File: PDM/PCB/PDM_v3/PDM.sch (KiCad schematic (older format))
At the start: 59 parts, among them IC1 SN74LVC1GU04DBVT, J1 12V BAT, J10 RASPBERRY PI, J11 EMU, J12 Conn_01x02_Male, J13 SAFETY SYSTEM, J16 GND, J2 EMU PIN 21 GN(AUX1), J3 EMU PIN 13 GN (AUX2), J4 BACK LIGHT, J5 COILS, J6 INJECTORS, J7 LSU 4.9, J8 RACE TCS, J9 STM BOX, U1 BTS50010-1TAE, U2 BTS50010-1TAE, U3 BTS50010-1TAE, U4 LM2937xMP

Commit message: Update PDM PCB
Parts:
- removed 12V1: 85 K1 (starter), MountingHole:MountingHole_2.5mm_Pad_Via, symbol Connector:Conn_01x01_Male
- removed C1: 0.2F, Kondensator:Kondensator, symbol Device:C
- removed C6: 0.1uF, Capacitor_SMD:C_0805_2012Metric, symbol Device:C_Small
- removed C7: 10uF, Capacitor_SMD:C_0805_2012Metric, symbol Device:C_Small
- removed D5: D_Schottky, Diode_SMD:D_SOD-123, symbol Device:D_Schottky
- removed IC1: SN74LVC1GU04DBVT, SN74LVC1GU04DBVT:SOT95P280X145-5N, symbol SN74LVC1GU04DBVT:SN74LVC1GU04DBVT
- removed J12: Conn_01x02_Male, Connector_PinHeader_2.54mm:PinHeader_1x02_P2.54mm_Vertical, symbol Connector:Conn_01x02_Male
- removed J13: SAFETY SYSTEM, MountingHole:MountingHole_2.2mm_M2_DIN965_Pad, symbol Connector:Conn_01x01_Male
- removed J2: EMU PIN 21 GN(AUX1), MountingHole:MountingHole_2.2mm_M2_DIN965_Pad, symbol Connector:Conn_01x01_Male
- removed J3: EMU PIN 13 GN (AUX2), MountingHole:MountingHole_2.2mm_M2_DIN965_Pad, symbol Connector:Conn_01x01_Male
- removed R1: 0.1, Resistor_SMD:R_0805_2012Metric, symbol Device:R
- removed U4: LM2937xMP, Package_TO_SOT_SMD:SOT-223-3_TabPin2, symbol Regulator_Linear:LM2937xMP
- added C1, C15, C17, C20, C55: 0.1uF, Capacitor_SMD:C_0603_1608Metric, symbol Device:C_Small
- added C27: 100nF, Capacitor_SMD:C_0805_2012Metric_Pad1.15x1.40mm_HandSolder, symbol Device:C
- added C28: 150nF, Capacitor_SMD:C_0603_1608Metric, symbol Device:C_Small
- added C29: 10nF, Capacitor_SMD:C_0805_2012Metric_Pad1.15x1.40mm_HandSolder, symbol Device:C
- added C30, C31: 100uF, EEETP1C101AP:EEE0JA471UAP, symbol EEETP1C101AP:EEETP1C101AP
- added C47, C54: 0.47uF, Capacitor_SMD:C_0603_1608Metric, symbol Device:C_Small
- added C48: 22uF, Capacitor_SMD:C_0603_1608Metric, symbol Device:C_Small
- added C49, C50: SCMR18H105PRBB0, SCMR18H105PRBB0:SCMR18H105PRBB0, symbol SCMR18H105PRBB0:SCMR18H105PRBB0
- added C51, C52, C56: 1uF, Capacitor_SMD:C_0603_1608Metric, symbol Device:C_Small
- added D9: D_TVS_ALT, Diode_SMD:D_SMA_Handsoldering, symbol Device:D_TVS_ALT
- added IC1, IC10, IC8: BU4S584G2-TR, BU4S584G2-TR:SOT95P280X125-5N, symbol BU4S584G2-TR:BU4S584G2-TR
- added IC7: KF50BDT-TR, KF50BDT-TR:TO228P972X240-3N, symbol KF50BDT-TR:KF50BDT-TR
- added IC9: TMP236A4DBZT, TMP236A4DBZT:SOT95P237X112-3N, symbol TMP236A4DBZT:TMP236A4DBZT
- added J15: SERVO_GEAR, MountingHole:MountingHole_2.2mm_M2_DIN965_Pad, symbol Connector:Conn_01x01_Male
- added J17: SERVO_CLUTCH, MountingHole:MountingHole_2.2mm_M2_DIN965_Pad, symbol Connector:Conn_01x01_Male
- added J2: 90130-1106, 90130-1106:SHDR6W65P254_2X3_996X975X1110P, symbol 90130-1106:90130-1106
- added J3: Conn_01x09_Male, Connector_PinHeader_1.27mm:PinHeader_1x09_P1.27mm_Vertical, symbol Connector:Conn_01x09_Male
- added R1: 22k, Resistor_SMD:R_0603_1608Metric, symbol Device:R_Small
- added R18: 1R, Resistor_SMD:R_0603_1608Metric_Pad1.05x0.95mm_HandSolder, symbol Device:R
- added R19: R_Small, Resistor_SMD:R_0603_1608Metric, symbol Device:R_Small
- added R20: R_Small, Resistor_SMD:R_1210_3225Metric, symbol Device:R_Small
- added R21: 6.8k, Resistor_SMD:R_0603_1608Metric, symbol Device:R_Small
- added R22, R23, R24, R25, R26, R27: 0, Resistor_SMD:R_0603_1608Metric, symbol Device:R_Small
- added SERVO1, SERVO2: 15, Fuse:Fuse_1206_3216Metric, symbol Device:Fuse
- added STM32: 2, Fuse:Fuse_0805_2012Metric, symbol Device:Fuse
- added U7: BTS50010-1TAE, Package_TO_SOT_SMD:TO-263-7_TabPin4, symbol PDM-rescue:BTS50010-1TAE-BTS50010-1TAE-PowerBox-rescue
- added U8: MCP2561-E-SN, Package_SO:SOIC-8_3.9x4.9mm_P1.27mm, symbol Interface_CAN_LIN:MCP2561-E-SN
- BACKLIGHT1: renamed from F2; footprint Fuse:Fuse_1812_4532Metric_Pad1.30x3.40mm_HandSolder -> Fuse:Fuse_1206_3216Metric
- COILS1: renamed from F3; footprint Fuse:Fuse_1812_4532Metric_Pad1.30x3.40mm_HandSolder -> Fuse:Fuse_1206_3216Metric
- DASHBOARD1: renamed from F7; footprint Fuse:Fuse_1812_4532Metric_Pad1.30x3.40mm_HandSolder -> Fuse:Fuse_1206_3216Metric
- EMU1: renamed from F9; footprint Fuse:Fuse_1812_4532Metric_Pad1.30x3.40mm_HandSolder -> Fuse:Fuse_1206_3216Metric
- H1, H2, H3, H4: footprint MountingHole:MountingHole_3.2mm_M3_DIN965_Pad -> MountingHole:MountingHole_3mm
- INJECTORS1: renamed from F4; footprint Fuse:Fuse_1812_4532Metric_Pad1.30x3.40mm_HandSolder -> Fuse:Fuse_1206_3216Metric
- J1, J16: footprint MountingHole:MountingHole_3.2mm_M3_Pad_Via -> MountingHole:MountingHole_4mm_Pad_Via
- J10: value RASPBERRY PI -> TELEM
- J4: value BACK LIGHT -> BACKLIGHT
- J9: value STM BOX -> DASHBOARD
- LSU1: renamed from F5; footprint Fuse:Fuse_1812_4532Metric_Pad1.30x3.40mm_HandSolder -> Fuse:Fuse_1206_3216Metric
- R2: value 100 -> 0; footprint Resistor_SMD:R_0805_2012Metric -> Resistor_SMD:R_0603_1608Metric
- R3, R4: value 10k -> 100k
- R6: value 100 -> 100k
- SPARE1: renamed from F6; footprint Fuse:Fuse_1812_4532Metric_Pad1.30x3.40mm_HandSolder -> Fuse:Fuse_1206_3216Metric
- TELEM1: renamed from F8; footprint Fuse:Fuse_1812_4532Metric_Pad1.30x3.40mm_HandSolder -> Fuse:Fuse_1206_3216Metric
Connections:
- net labels added: +5V, 12V_MAIN_IN, 12V_MAIN_OUT, 12V_SERVO_OUT, 12V_STM32, 12V_SYSTEMS, 12V_SYSTEMS_OUT, 5V_ST_LINK, CAN_H, CAN_L, CAN_RX, CAN_TX, CURRENT_12V_MAIN, CURRENT_12V_SYSTEMS, CURRENT_FANS, CURRENT_FUEL, CURRENT_SERVO, EMU_AUX1, EMU_AUX2, FANS_MOS_IN, FANS_MOS_OUT, FUEL_MOS_IN, FUEL_MOS_OUT, IN_FAN, IN_FUEL, IN_MAIN_12V, IN_MAIN_SYS, SAFETY_LINE, TEMP, VOLTAGE_SENS
- net labels removed: BRAKE_SWITCH, BSPD_IN, IN_1, IN_2, IN_3
- wire segments 121 -> 277
- no-connect marks 3 -> 5
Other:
- note added: "14V MAX -> 3.3V MAX"
- note added: "3.3V buck"
- note added: "5V LDO"
- note added: "CAN BUS"
- note added: "Control Fans MOS"
- note added: "Control Fuel Pump MOS"
- note added: "Control Main power MOS"
- note added: "MAIN"
- note added: "MAIN CURRENT SENSING"
- note added: "STM32"
- note added: "SYSTEMS"
- note added: "SYSTEMS CURRENT SENSING"
- note added: "TEMP SENSOR"
- note added: "VOLTAGE SENSOR"
- moved on the sheet: BACKLIGHT1, C10, C11, C12, C2, C3, C4, C5, C8, C9, COILS1, D1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

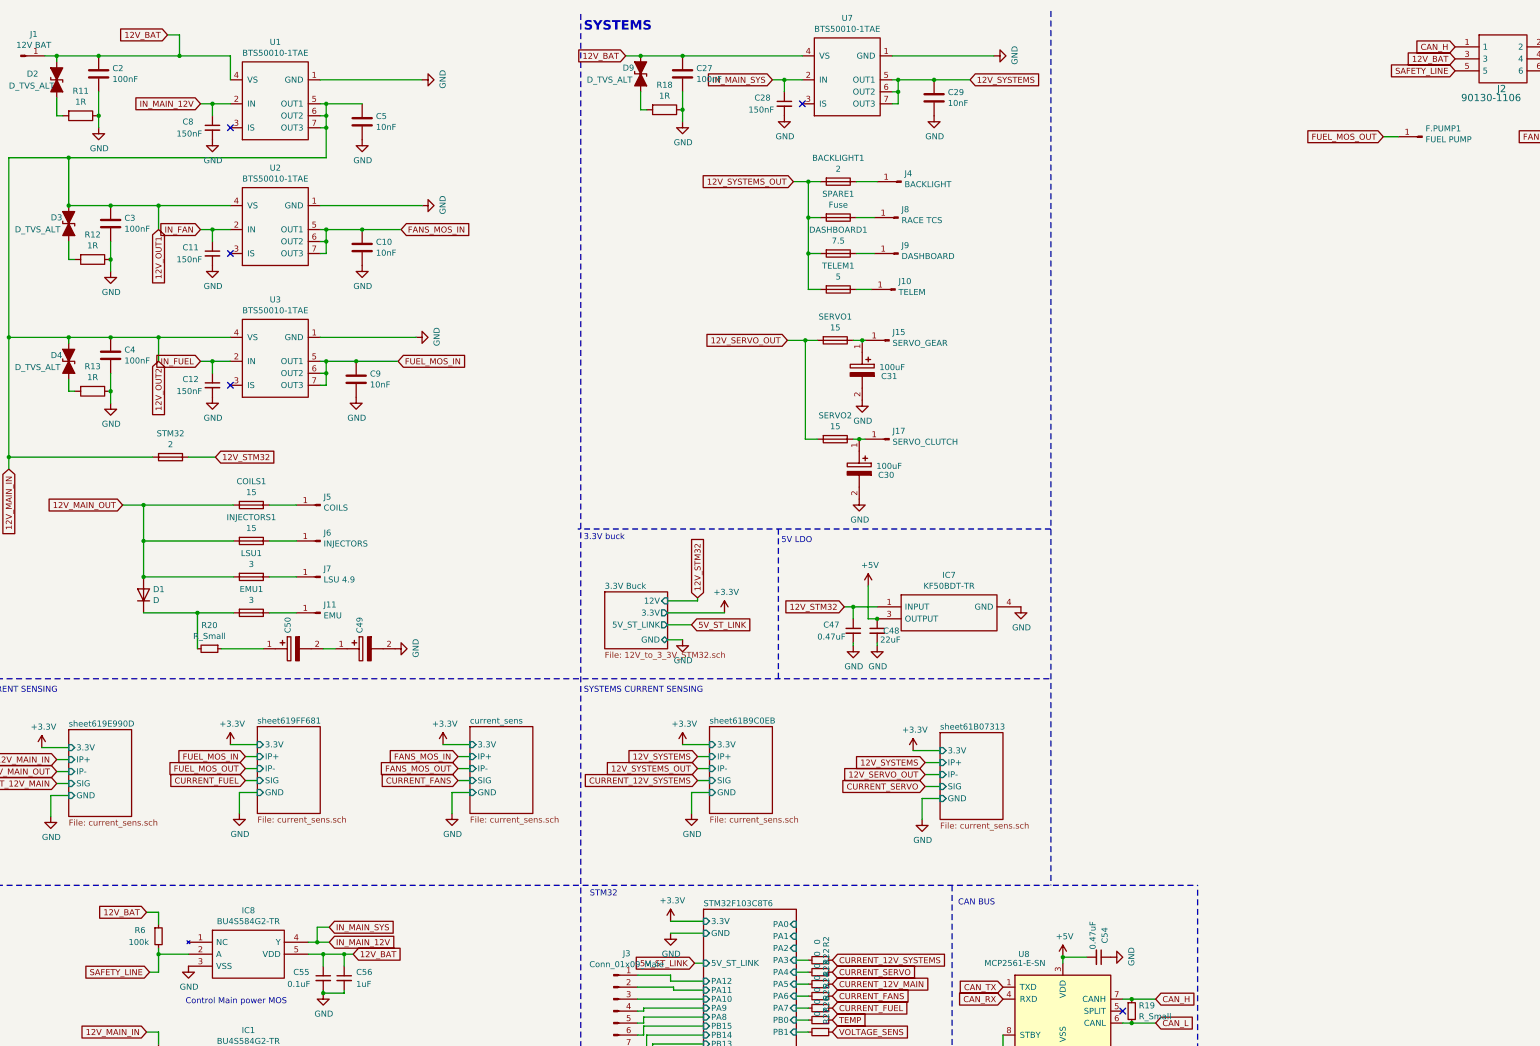
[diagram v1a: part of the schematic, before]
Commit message: Add PCB for PDM
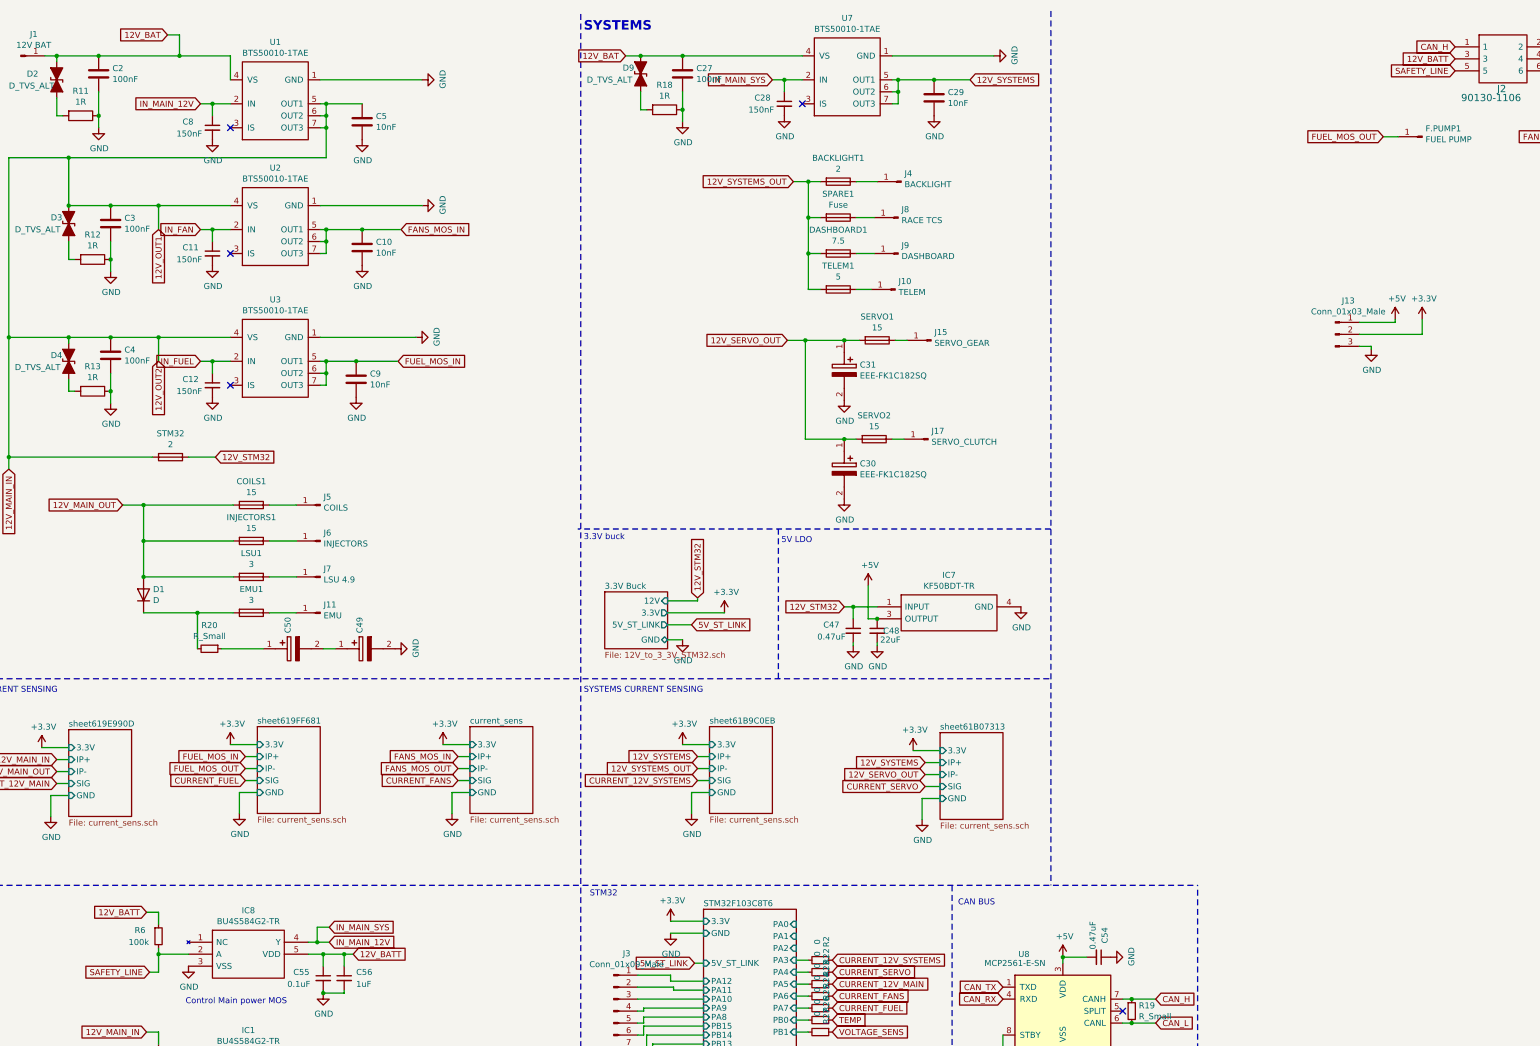
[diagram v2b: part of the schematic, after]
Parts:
- removed C30, C31: 100uF, EEETP1C101AP:EEE0JA471UAP, symbol EEETP1C101AP:EEETP1C101AP
- added C30, C31: EEE-FK1C182SQ, EEE-FK1C182SQ:EEEFK0J332AQ, symbol EEE-FK1C182SQ:EEE-FK1C182SQ
- added J13: Conn_01x03_Male, Connector_PinHeader_2.54mm:PinHeader_1x03_P2.54mm_Vertical, symbol Connector:Conn_01x03_Male
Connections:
- net +3V3: now also J13.2 (Pin_2)
- net +5V: now also J13.1 (Pin_1)
- net 12V_BAT: no longer C55.1, C56.1, IC8.5 (VDD), J2.3, R6.1
- net 12V_SERVO_OUT: now also C30.1, C31.1
- net GND: now also C30.2, C31.2, J13.3 (Pin_3)
- new net 12V_BATT: C55.1, C56.1, IC8.5 (VDD), J2.3, R6.1
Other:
- moved on the sheet: J15, J17, SERVO1, SERVO2
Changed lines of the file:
@@
 L Connector:Conn_01x01_Male J15
 U 1 1 61AA1863
-P 8325 3225
-F 0 "J15" H 8297 3157 50  0000 R CNN
-F 1 "SERVO_GEAR" H 8297 3248 50  0000 R CNN
-F 2 "MountingHole:MountingHole_2.2mm_M2_DIN965_Pad" H 8325 3225 50  0001 C CNN
-F 3 "~" H 8325 3225 50  0001 C CNN
-	1    8325 3225
+P 8675 3225
+F 0 "J15" H 8647 3157 50  0000 R CNN
+F 1 "SERVO_GEAR" H 8647 3248 50  0000 R CNN
+F 2 "MountingHole:MountingHole_2.2mm_M2_DIN965_Pad" H 8675 3225 50  0001 C CNN
+F 3 "~" H 8675 3225 50  0001 C CNN
+	1    8675 3225
 	-1   0    0    1
 $EndComp
@@
 L Connector:Conn_01x01_Male J17
 U 1 1 61AA1C4E
-P 8325 4050
-F 0 "J17" H 8297 3982 50  0000 R CNN
-F 1 "SERVO_CLUTCH" H 8297 4073 50  0000 R CNN
-F 2 "MountingHole:MountingHole_2.2mm_M2_DIN965_Pad" H 8325 4050 50  0001 C CNN
-F 3 "~" H 8325 4050 50  0001 C CNN
-	1    8325 4050
+P 8650 4050
+F 0 "J17" H 8622 3982 50  0000 R CNN
+F 1 "SERVO_CLUTCH" H 8622 4073 50  0000 R CNN
+F 2 "MountingHole:MountingHole_2.2mm_M2_DIN965_Pad" H 8650 4050 50  0001 C CNN
+F 3 "~" H 8650 4050 50  0001 C CNN
+	1    8650 4050
 	-1   0    0    1
 $EndComp
-Wire Wire Line
-	8025 3225 8100 3225
-Connection ~ 8100 3225
-Wire Wire Line
-	8100 3225 8125 3225
 $Sheet
 S 4825 6450 525  725
@@
 12V_SERVO_OUT
 Wire Wire Line
-	7725 4050 7625 4050
-Wire Wire Line
 	7625 4050 7625 3225
-Wire Wire Line
-	7625 3225 7725 3225
 Text GLabel 8625 6850 0    50   Input ~ 0
 12V_SERVO_OUT
@@
 L power:GND #PWR063
 U 1 1 6193D55B
-P 8100 3725
-F 0 "#PWR063" H 8100 3475 50  0001 C CNN
-F 1 "GND" H 8105 3552 50  0000 C CNN
-F 2 "" H 8100 3725 50  0001 C CNN
-F 3 "" H 8100 3725 50  0001 C CNN
-	1    8100 3725
-	1    0    0    -1
-$EndComp
-Connection ~ 8075 4050
-Wire Wire Line
-	8075 4050 8125 4050
-Wire Wire Line
-	8025 4050 8075 4050
+P 7950 3725
+F 0 "#PWR063" H 7950 3475 50  0001 C CNN
+F 1 "GND" H 7955 3552 50  0000 C CNN
+F 2 "" H 7950 3725 50  0001 C CNN
+F 3 "" H 7950 3725 50  0001 C CNN
+	1    7950 3725
+	1    0    0    -1
+$EndComp
 $Comp
 L power:GND #PWR062
 U 1 1 6193FE29
-P 8075 4550
-F 0 "#PWR062" H 8075 4300 50  0001 C CNN
-F 1 "GND" H 8080 4377 50  0000 C CNN
-F 2 "" H 8075 4550 50  0001 C CNN
-F 3 "" H 8075 4550 50  0001 C CNN
-	1    8075 4550
-	1    0    0    -1
-$EndComp
-$Comp
-L EEETP1C101AP:EEETP1C101AP C30
-U 1 1 6193FE23
-P 8075 4050
-F 0 "C30" V 8375 4275 50  0000 C CNN
-F 1 "100uF" V 8300 4300 50  0000 C CNN
-F 2 "EEETP1C101AP:EEE0JA471UAP" H 8425 4100 50  0001 L CNN
-F 3 "http://industrial.panasonic.com/cdbs/www-data/pdf/RDE0000/ABA0000C1196.pdf" H 8425 4000 50  0001 L CNN
-F 4 "Panasonic 100F 16V dc Aluminium Electrolytic Capacitor, Surface Mount 8 (Dia.) x 10.2mm +125C 8mm 3.1mm" H 8425 3900 50  0001 L CNN "Description"
-F 5 "10" H 8425 3800 50  0001 L CNN "Height"
-F 6 "Panasonic" H 8425 3700 50  0001 L CNN "Manufacturer_Name"
-F 7 "EEETP1C101AP" H 8425 3600 50  0001 L CNN "Manufacturer_Part_Number"
-F 8 "" H 8425 3500 50  0001 L CNN "Mouser Part Number"
-F 9 "" H 8425 3400 50  0001 L CNN "Mouser Price/Stock"
-F 10 "EEETP1C101AP" H 8425 3300 50  0001 L CNN "Arrow Part Number"
-F 11 "https://www.arrow.com/en/products/eee-tp1c101ap/panasonic" H 8425 3200 50  0001 L CNN "Arrow Price/Stock"
-	1    8075 4050
-	0    1    1    0
+P 7950 4550
+F 0 "#PWR062" H 7950 4300 50  0001 C CNN
+F 1 "GND" H 7955 4377 50  0000 C CNN
+F 2 "" H 7950 4550 50  0001 C CNN
+F 3 "" H 7950 4550 50  0001 C CNN
+	1    7950 4550
+	1    0    0    -1
 $EndComp
 $Comp
@@
 L Device:Fuse SERVO2
 U 1 1 61AA13A7
-P 7875 4050
-F 0 "SERVO2" V 7678 4050 50  0000 C CNN
-F 1 "15" V 7769 4050 50  0000 C CNN
-F 2 "Fuse:Fuse_1206_3216Metric" V 7805 4050 50  0001 C CNN
-F 3 "~" H 7875 4050 50  0001 C CNN
-	1    7875 4050
+P 8200 4050
+F 0 "SERVO2" V 8003 4050 50  0000 C CNN
+F 1 "15" V 8094 4050 50  0000 C CNN
+F 2 "Fuse:Fuse_1206_3216Metric" V 8130 4050 50  0001 C CNN
+F 3 "~" H 8200 4050 50  0001 C CNN
+	1    8200 4050
 	0    1    1    0
 $EndComp
@@
 L Device:Fuse SERVO1
 U 1 1 61AA1007
-P 7875 3225
-F 0 "SERVO1" V 7678 3225 50  0000 C CNN
-F 1 "15" V 7769 3225 50  0000 C CNN
-F 2 "Fuse:Fuse_1206_3216Metric" V 7805 3225 50  0001 C CNN
-F 3 "~" H 7875 3225 50  0001 C CNN
-	1    7875 3225
-	0    1    1    0
-$EndComp
-$Comp
-L EEETP1C101AP:EEETP1C101AP C31
-U 1 1 61ADEF9B
-P 8100 3225
-F 0 "C31" V 8400 3450 50  0000 C CNN
-F 1 "100uF" V 8325 3475 50  0000 C CNN
-F 2 "EEETP1C101AP:EEE0JA471UAP" H 8450 3275 50  0001 L CNN
-F 3 "http://industrial.panasonic.com/cdbs/www-data/pdf/RDE0000/ABA0000C1196.pdf" H 8450 3175 50  0001 L CNN
-F 4 "Panasonic 100F 16V dc Aluminium Electrolytic Capacitor, Surface Mount 8 (Dia.) x 10.2mm +125C 8mm 3.1mm" H 8450 3075 50  0001 L CNN "Description"
-F 5 "10" H 8450 2975 50  0001 L CNN "Height"
-F 6 "Panasonic" H 8450 2875 50  0001 L CNN "Manufacturer_Name"
-F 7 "EEETP1C101AP" H 8450 2775 50  0001 L CNN "Manufacturer_Part_Number"
-F 8 "" H 8450 2675 50  0001 L CNN "Mouser Part Number"
-F 9 "" H 8450 2575 50  0001 L CNN "Mouser Price/Stock"
-F 10 "EEETP1C101AP" H 8450 2475 50  0001 L CNN "Arrow Part Number"
-F 11 "https://www.arrow.com/en/products/eee-tp1c101ap/panasonic" H 8450 2375 50  0001 L CNN "Arrow Price/Stock"
-	1    8100 3225
+P 8225 3225
+F 0 "SERVO1" V 8028 3225 50  0000 C CNN
+F 1 "15" V 8119 3225 50  0000 C CNN
+F 2 "Fuse:Fuse_1206_3216Metric" V 8155 3225 50  0001 C CNN
+F 3 "~" H 8225 3225 50  0001 C CNN
+	1    8225 3225
 	0    1    1    0
 $EndComp
@@
 $EndComp
 Text GLabel 2125 8000 0    50   Input ~ 0
-12V_BAT
+12V_BATT
 Wire Wire Line
 	2125 8000 2225 8000
 Text GLabel 3850 8350 2    50   Input ~ 0
-12V_BAT
+12V_BATT
 $Comp
 L Device:C_Small C56
@@
 14V MAX -> 3.3V MAX
 Text GLabel 13050 875  0    50   Input ~ 0
-12V_BAT
+12V_BATT
 $Comp
 L TMP236A4DBZT:TMP236A4DBZT IC9
@@
 Text GLabel 3850 10425 2    50   Input ~ 0
 12V_MAIN_IN
+$Comp
+L EEE-FK1C182SQ:EEE-FK1C182SQ C31
+U 1 1 61F15847
+P 7950 3225
+F 0 "C31" V 8154 3355 50  0000 L CNN
+F 1 "EEE-FK1C182SQ" V 8245 3355 50  0000 L CNN
+F 2 "EEE-FK1C182SQ:EEEFK0J332AQ" H 8300 3275 50  0001 L CNN
+F 3 "http://industrial.panasonic.com/cdbs/www-data/pdf/RDE0000/ABA0000C1247.pdf" H 8300 3175 50  0001 L CNN
+F 4 "Aluminum Electrolytic Capacitors - SMD 16VDC 1800uF 20% 12.5x13.5mm AEC-Q200" H 8300 3075 50  0001 L CNN "Description"
+F 5 "15" H 8300 2975 50  0001 L CNN "Height"
+F 6 "Panasonic" H 8300 2875 50  0001 L CNN "Manufacturer_Name"
+F 7 "EEE-FK1C182SQ" H 8300 2775 50  0001 L CNN "Manufacturer_Part_Number"
+F 8 "667-EEE-FK1C182SQ" H 8300 2675 50  0001 L CNN "Mouser Part Number"
+F 9 "https://www.mouser.co.uk/ProductDetail/Panasonic/EEE-FK1C182SQ?qs=BZBei1rCqCDZ%2F9wPPM5YoA%3D%3D" H 8300 2575 50  0001 L CNN "Mouser Price/Stock"
+F 10 "EEE-FK1C182SQ" H 8300 2475 50  0001 L CNN "Arrow Part Number"
+F 11 "https://www.arrow.com/en/products/eee-fk1c182sq/panasonic" H 8300 2375 50  0001 L CNN "Arrow Price/Stock"
+	1    7950 3225
+	0    1    1    0
+$EndComp
+$Comp
+L EEE-FK1C182SQ:EEE-FK1C182SQ C30
+U 1 1 61F16639
+P 7950 4050
+F 0 "C30" V 8154 4180 50  0000 L CNN
+F 1 "EEE-FK1C182SQ" V 8245 4180 50  0000 L CNN
+F 2 "EEE-FK1C182SQ:EEEFK0J332AQ" H 8300 4100 50  0001 L CNN
+F 3 "http://industrial.panasonic.com/cdbs/www-data/pdf/RDE0000/ABA0000C1247.pdf" H 8300 4000 50  0001 L CNN
+F 4 "Aluminum Electrolytic Capacitors - SMD 16VDC 1800uF 20% 12.5x13.5mm AEC-Q200" H 8300 3900 50  0001 L CNN "Description"
+F 5 "15" H 8300 3800 50  0001 L CNN "Height"
+F 6 "Panasonic" H 8300 3700 50  0001 L CNN "Manufacturer_Name"
+F 7 "EEE-FK1C182SQ" H 8300 3600 50  0001 L CNN "Manufacturer_Part_Number"
+F 8 "667-EEE-FK1C182SQ" H 8300 3500 50  0001 L CNN "Mouser Part Number"
+F 9 "https://www.mouser.co.uk/ProductDetail/Panasonic/EEE-FK1C182SQ?qs=BZBei1rCqCDZ%2F9wPPM5YoA%3D%3D" H 8300 3400 50  0001 L CNN "Mouser Price/Stock"
+F 10 "EEE-FK1C182SQ" H 8300 3300 50  0001 L CNN "Arrow Part Number"
+F 11 "https://www.arrow.com/en/products/eee-fk1c182sq/panasonic" H 8300 3200 50  0001 L CNN "Arrow Price/Stock"
+	1    7950 4050
+	0    1    1    0
+$EndComp
+Wire Wire Line
+	8350 4050 8450 4050
+Wire Wire Line
+	8375 3225 8475 3225
+Wire Wire Line
+	7625 3225 7950 3225
+Connection ~ 7950 3225
+Wire Wire Line
+	7950 3225 8075 3225
+Wire Wire Line
+	7625 4050 7950 4050
+Connection ~ 7950 4050
+Wire Wire Line
+	7950 4050 8050 4050
+$Comp
+L Connector:Conn_01x03_Male J13
+U 1 1 61F8AC8A
+P 12050 3175
+F 0 "J13" H 12158 3456 50  0000 C CNN
+F 1 "Conn_01x03_Male" H 12158 3365 50  0000 C CNN
+F 2 "Connector_PinHeader_2.54mm:PinHeader_1x03_P2.54mm_Vertical" H 12050 3175 50  0001 C CNN
+F 3 "~" H 12050 3175 50  0001 C CNN
+	1    12050 3175
+	1    0    0    -1
+$EndComp
+$Comp
+L power:+5V #PWR0125
+U 1 1 61FAAFEC
+P 12550 3050
+F 0 "#PWR0125" H 12550 2900 50  0001 C CNN
+F 1 "+5V" H 12565 3223 50  0000 C CNN
+F 2 "" H 12550 3050 50  0001 C CNN
+F 3 "" H 12550 3050 50  0001 C CNN
+	1    12550 3050
+	1    0    0    -1
+$EndComp
+Wire Wire Line
+	12250 3075 12550 3075
+Wire Wire Line
+	12550 3075 12550 3050
+$Comp
+L power:+3.3V #PWR0126
+U 1 1 61FE17FF
+P 12775 3050
+F 0 "#PWR0126" H 12775 2900 50  0001 C CNN
+F 1 "+3.3V" H 12790 3223 50  0000 C CNN
+F 2 "" H 12775 3050 50  0001 C CNN
+F 3 "" H 12775 3050 50  0001 C CNN
+	1    12775 3050
+	1    0    0    -1
+$EndComp
+Wire Wire Line
+	12775 3050 12775 3175
+Wire Wire Line
+	12775 3175 12250 3175
+$Comp
+L power:GND #PWR0127
+U 1 1 61FF928B
+P 12350 3300
+F 0 "#PWR0127" H 12350 3050 50  0001 C CNN
+F 1 "GND" H 12355 3127 50  0000 C CNN
+F 2 "" H 12350 3300 50  0001 C CNN
+F 3 "" H 12350 3300 50  0001 C CNN
+	1    12350 3300
+	1    0    0    -1
+$EndComp
+Wire Wire Line
+	12350 3300 12350 3275
+Wire Wire Line
+	12350 3275 12250 3275
 $EndSCHEMATC
